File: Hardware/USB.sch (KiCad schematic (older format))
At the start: 11 parts

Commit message: [Hardware] Added USB-B connector reference and 3D model.
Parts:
- J1: renamed from J?; value USB_B -> 2411_06; Manufacturer (none) -> Lumberg
- gave numbers to parts that had none: 10
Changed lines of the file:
@@
 P 6600 3950
 AR Path="/61165087" Ref="U?"  Part="1"
-AR Path="/611612DA/61165087" Ref="U?"  Part="1"
-F 0 "U?" H 7000 3300 50  0000 C CNN
+AR Path="/611612DA/61165087" Ref="U1"  Part="1"
+F 0 "U1" H 7000 3300 50  0000 C CNN
 F 1 "FT230XS" H 7100 3200 50  0000 C CNN
 F 2 "Package_SO:SSOP-16_3.9x4.9mm_P0.635mm" H 7600 3350 50  0001 C CNN
@@
 P 4700 3850
 AR Path="/6116508E" Ref="R?"  Part="1"
-AR Path="/611612DA/6116508E" Ref="R?"  Part="1"
-F 0 "R?" V 4403 3850 50  0000 C CNN
+AR Path="/611612DA/6116508E" Ref="R1"  Part="1"
+F 0 "R1" V 4403 3850 50  0000 C CNN
 F 1 "27" V 4494 3850 50  0000 C CNN
 F 2 "Resistor_SMD:R_0603_1608Metric_Pad0.98x0.95mm_HandSolder" V 4630 3850 50  0001 C CNN
@@
 P 4700 3950
 AR Path="/61165095" Ref="R?"  Part="1"
-AR Path="/611612DA/61165095" Ref="R?"  Part="1"
-F 0 "R?" V 4815 3950 50  0000 C CNN
+AR Path="/611612DA/61165095" Ref="R2"  Part="1"
+F 0 "R2" V 4815 3950 50  0000 C CNN
 F 1 "27" V 4906 3950 50  0000 C CNN
 F 2 "Resistor_SMD:R_0603_1608Metric_Pad0.98x0.95mm_HandSolder" V 4630 3950 50  0001 C CNN
@@
 P 3900 4500
 AR Path="/6116509D" Ref="C?"  Part="1"
-AR Path="/611612DA/6116509D" Ref="C?"  Part="1"
-F 0 "C?" H 3786 4637 50  0000 R CNN
+AR Path="/611612DA/6116509D" Ref="C6"  Part="1"
+F 0 "C6" H 3786 4637 50  0000 R CNN
 F 1 "47p" H 3786 4546 50  0000 R CNN
 F 2 "Capacitor_SMD:C_0603_1608Metric_Pad1.08x0.95mm_HandSolder" H 3938 4350 50  0001 C CNN
@@
 P 4200 4500
 AR Path="/611650A5" Ref="C?"  Part="1"
-AR Path="/611612DA/611650A5" Ref="C?"  Part="1"
-F 0 "C?" H 4315 4637 50  0000 L CNN
+AR Path="/611612DA/611650A5" Ref="C7"  Part="1"
+F 0 "C7" H 4315 4637 50  0000 L CNN
 F 1 "47p" H 4315 4546 50  0000 L CNN
 F 2 "Capacitor_SMD:C_0603_1608Metric_Pad1.08x0.95mm_HandSolder" H 4238 4350 50  0001 C CNN
@@
 P 2900 3850
 AR Path="/611650AB" Ref="J?"  Part="1"
-AR Path="/611612DA/611650AB" Ref="J?"  Part="1"
-F 0 "J?" H 2957 4317 50  0000 C CNN
-F 1 "USB_B" H 2957 4226 50  0000 C CNN
+AR Path="/611612DA/611650AB" Ref="J1"  Part="1"
+F 0 "J1" H 2957 4317 50  0000 C CNN
+F 1 "2411_06" H 2957 4226 50  0000 C CNN
 F 2 "Connector_USB:USB_B_OST_USB-B1HSxx_Horizontal" H 3050 3800 50  0001 C CNN
 F 3 " ~" H 3050 3800 50  0001 C CNN
+F 4 "Lumberg" H 2900 3850 50  0001 C CNN "Manufacturer"
 	1    2900 3850
 	1    0    0    -1
 $EndComp
 $Comp
-L power:GND #PWR?
+L power:GND #PWR09
 U 1 1 61168B65
 P 6600 4800
-F 0 "#PWR?" H 6600 4550 50  0001 C CNN
+F 0 "#PWR09" H 6600 4550 50  0001 C CNN
 F 1 "GND" H 6605 4627 50  0000 C CNN
 F 2 "" H 6600 4800 50  0001 C CNN
@@
 Connection ~ 6600 4750
 $Comp
-L power:GND #PWR?
+L power:GND #PWR010
 U 1 1 61169C53
 P 4050 4850
-F 0 "#PWR?" H 4050 4600 50  0001 C CNN
+F 0 "#PWR010" H 4050 4600 50  0001 C CNN
 F 1 "GND" H 4055 4677 50  0000 C CNN
 F 2 "" H 4050 4850 50  0001 C CNN
@@
 USB_2_D+
 $Comp
-L power:GND #PWR?
+L power:GND #PWR08
 U 1 1 61185C32
 P 2850 4350
-F 0 "#PWR?" H 2850 4100 50  0001 C CNN
+F 0 "#PWR08" H 2850 4100 50  0001 C CNN
 F 1 "GND" H 2855 4177 50  0000 C CNN
 F 2 "" H 2850 4350 50  0001 C CNN
@@
 Connection ~ 2850 4300
 $Comp
-L power:+5V #PWR?
+L power:+5V #PWR05
 U 1 1 6118716E
 P 3300 3300
-F 0 "#PWR?" H 3300 3150 50  0001 C CNN
+F 0 "#PWR05" H 3300 3150 50  0001 C CNN
 F 1 "+5V" H 3315 3473 50  0000 C CNN
 F 2 "" H 3300 3300 50  0001 C CNN
@@
 P 6050 2600
 AR Path="/611938BC" Ref="C?"  Part="1"
-AR Path="/611612DA/611938BC" Ref="C?"  Part="1"
-F 0 "C?" H 6165 2737 50  0000 L CNN
+AR Path="/611612DA/611938BC" Ref="C4"  Part="1"
+F 0 "C4" H 6165 2737 50  0000 L CNN
 F 1 "4.7u" H 6165 2646 50  0000 L CNN
 F 2 "Capacitor_SMD:C_0805_2012Metric_Pad1.18x1.45mm_HandSolder" H 6088 2450 50  0001 C CNN
@@
 P 5500 2600
 AR Path="/61195755" Ref="C?"  Part="1"
-AR Path="/611612DA/61195755" Ref="C?"  Part="1"
-F 0 "C?" H 5615 2737 50  0000 L CNN
+AR Path="/611612DA/61195755" Ref="C3"  Part="1"
+F 0 "C3" H 5615 2737 50  0000 L CNN
 F 1 "4.7u" H 5615 2646 50  0000 L CNN
 F 2 "Capacitor_SMD:C_0805_2012Metric_Pad1.18x1.45mm_HandSolder" H 5538 2450 50  0001 C CNN
@@
 P 4950 2600
 AR Path="/61196FE9" Ref="C?"  Part="1"
-AR Path="/611612DA/61196FE9" Ref="C?"  Part="1"
-F 0 "C?" H 5065 2737 50  0000 L CNN
+AR Path="/611612DA/61196FE9" Ref="C2"  Part="1"
+F 0 "C2" H 5065 2737 50  0000 L CNN
 F 1 "100n" H 5065 2646 50  0000 L CNN
 F 2 "Capacitor_SMD:C_0603_1608Metric_Pad1.08x0.95mm_HandSolder" H 4988 2450 50  0001 C CNN
@@
 P 4400 2600
 AR Path="/6119756B" Ref="C?"  Part="1"
-AR Path="/611612DA/6119756B" Ref="C?"  Part="1"
-F 0 "C?" H 4515 2737 50  0000 L CNN
+AR Path="/611612DA/6119756B" Ref="C1"  Part="1"
+F 0 "C1" H 4515 2737 50  0000 L CNN
 F 1 "100n" H 4515 2646 50  0000 L CNN
 F 2 "Capacitor_SMD:C_0603_1608Metric_Pad1.08x0.95mm_HandSolder" H 4438 2450 50  0001 C CNN
@@
 $EndComp
 $Comp
-L power:+5V #PWR?
+L power:+5V #PWR01
 U 1 1 611A0261
 P 4400 2250
-F 0 "#PWR?" H 4400 2100 50  0001 C CNN
+F 0 "#PWR01" H 4400 2100 50  0001 C CNN
 F 1 "+5V" H 4415 2423 50  0000 C CNN
 F 2 "" H 4400 2250 50  0001 C CNN
@@
 	6500 2350 6500 3250
 $Comp
-L power:GND #PWR?
+L power:GND #PWR04
 U 1 1 611A5DF9
 P 5250 2950
-F 0 "#PWR?" H 5250 2700 50  0001 C CNN
+F 0 "#PWR04" H 5250 2700 50  0001 C CNN
 F 1 "GND" H 5255 2777 50  0000 C CNN
 F 2 "" H 5250 2950 50  0001 C CNN
@@
 	5250 2850 5500 2850
 $Comp
-L power:+3.3VA #PWR?
+L power:+3.3VA #PWR02
 U 1 1 611A8920
 P 7100 2250
-F 0 "#PWR?" H 7100 2100 50  0001 C CNN
+F 0 "#PWR02" H 7100 2100 50  0001 C CNN
 F 1 "+3.3VA" H 7115 2423 50  0000 C CNN
 F 2 "" H 7100 2250 50  0001 C CNN
@@
 P 7100 2600
 AR Path="/611A99B1" Ref="C?"  Part="1"
-AR Path="/611612DA/611A99B1" Ref="C?"  Part="1"
-F 0 "C?" H 7215 2737 50  0000 L CNN
+AR Path="/611612DA/611A99B1" Ref="C5"  Part="1"
+F 0 "C5" H 7215 2737 50  0000 L CNN
 F 1 "100n" H 7215 2646 50  0000 L CNN
 F 2 "Capacitor_SMD:C_0603_1608Metric_Pad1.08x0.95mm_HandSolder" H 7138 2450 50  0001 C CNN
@@
 Connection ~ 7100 2350
 $Comp
-L power:GND #PWR?
+L power:GND #PWR03
 U 1 1 611ACC4D
 P 7100 2850
-F 0 "#PWR?" H 7100 2600 50  0001 C CNN
+F 0 "#PWR03" H 7100 2600 50  0001 C CNN
 F 1 "GND" H 7105 2677 50  0000 C CNN
 F 2 "" H 7100 2850 50  0001 C CNN
@@
 	7100 2850 7100 2750
 $Comp
-L power:+3.3VA #PWR?
+L power:+3.3VA #PWR06
 U 1 1 611AF903
 P 5800 3550
-F 0 "#PWR?" H 5800 3400 50  0001 C CNN
+F 0 "#PWR06" H 5800 3400 50  0001 C CNN
 F 1 "+3.3VA" V 5815 3677 50  0000 L CNN
 F 2 "" H 5800 3550 50  0001 C CNN
@@
 $EndComp
 $Comp
-L power:+3.3VA #PWR?
+L power:+3.3VA #PWR07
 U 1 1 611B03B1
 P 5800 4150
-F 0 "#PWR?" H 5800 4000 50  0001 C CNN
+F 0 "#PWR07" H 5800 4000 50  0001 C CNN
 F 1 "+3.3VA" V 5815 4277 50  0000 L CNN
 F 2 "" H 5800 4150 50  0001 C CNN

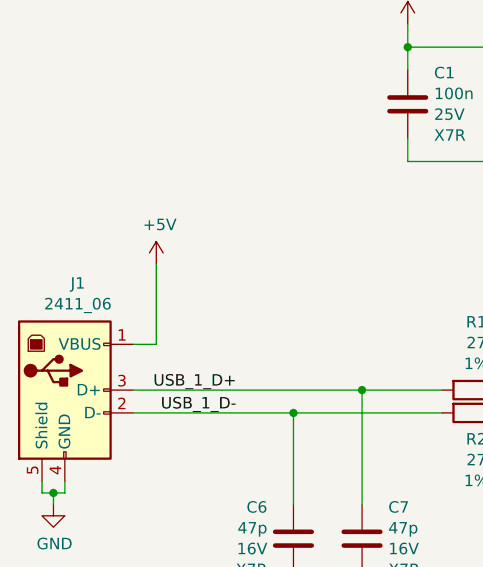
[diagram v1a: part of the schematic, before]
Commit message: [Hardware] Added relays schematic sheet.
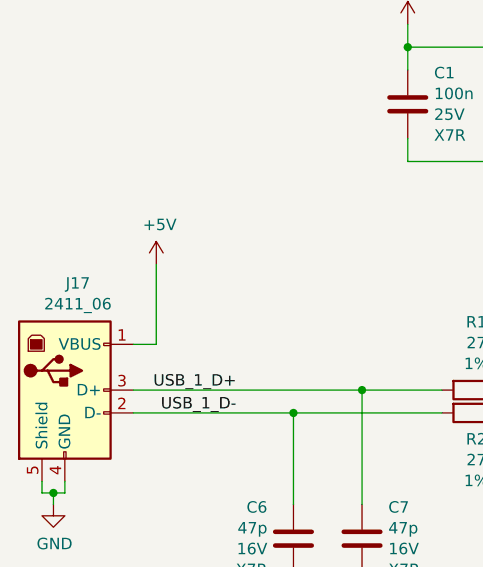
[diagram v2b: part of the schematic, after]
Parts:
- renumbered J1 to J17
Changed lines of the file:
@@
 P 2900 3850
 AR Path="/611650AB" Ref="J?"  Part="1"
-AR Path="/611612DA/611650AB" Ref="J1"  Part="1"
-F 0 "J1" H 2957 4317 50  0000 C CNN
+AR Path="/611612DA/611650AB" Ref="J17"  Part="1"
+F 0 "J17" H 2957 4317 50  0000 C CNN
 F 1 "2411_06" H 2957 4226 50  0000 C CNN
 F 2 "Connector_USB:USB_B_OST_USB-B1HSxx_Horizontal" H 3050 3800 50  0001 C CNN

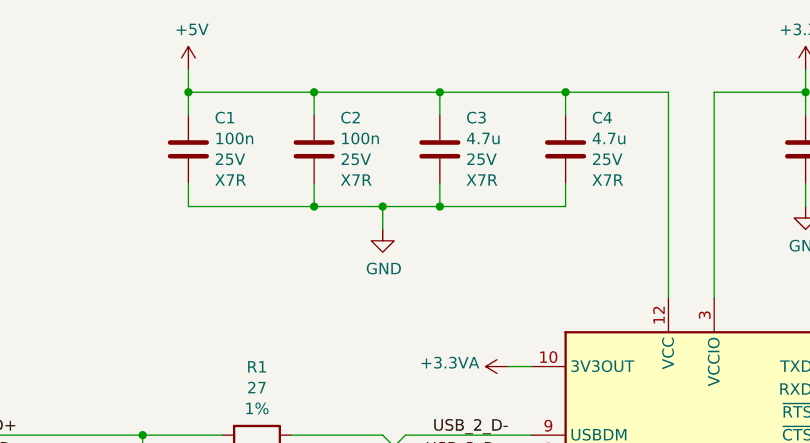
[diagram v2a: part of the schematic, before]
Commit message: [Hardware] Positioned components on PCB.
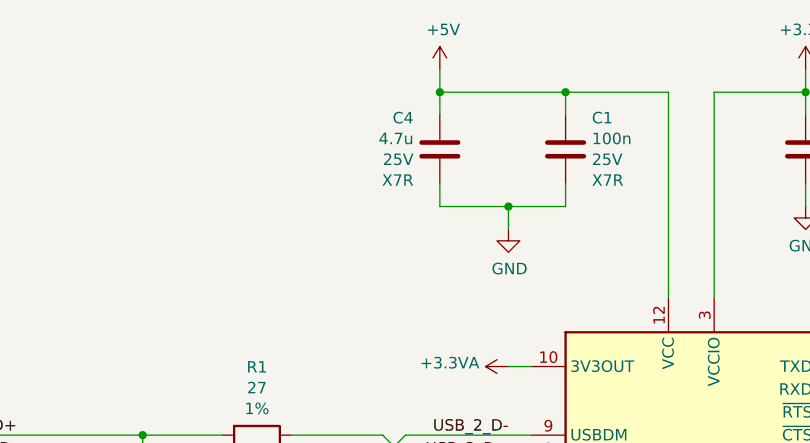
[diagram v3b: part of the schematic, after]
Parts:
- removed C2: 100n, Capacitor_SMD:C_0603_1608Metric_Pad1.08x0.95mm_HandSolder, symbol Device:C
- removed C3: 4.7u, Capacitor_SMD:C_0805_2012Metric_Pad1.18x1.45mm_HandSolder, symbol Device:C
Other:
- moved on the sheet: C1, C4
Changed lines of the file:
@@
 L Device:C C?
 U 1 1 611938BC
-P 6050 2600
+P 5500 2600
 AR Path="/611938BC" Ref="C?"  Part="1"
 AR Path="/611612DA/611938BC" Ref="C4"  Part="1"
-F 0 "C4" H 6165 2737 50  0000 L CNN
-F 1 "4.7u" H 6165 2646 50  0000 L CNN
-F 2 "Capacitor_SMD:C_0805_2012Metric_Pad1.18x1.45mm_HandSolder" H 6088 2450 50  0001 C CNN
+F 0 "C4" H 5385 2737 50  0000 R CNN
+F 1 "4.7u" H 5385 2646 50  0000 R CNN
+F 2 "Capacitor_SMD:C_0805_2012Metric_Pad1.18x1.45mm_HandSolder" H 5538 2450 50  0001 C CNN
+F 3 "~" H 5500 2600 50  0001 C CNN
+F 4 "25V" H 5385 2555 50  0000 R CNN "Value2"
+F 5 "X7R" H 5385 2464 50  0000 R CNN "Value3"
+	1    5500 2600
+	1    0    0    -1
+$EndComp
+$Comp
+L Device:C C?
+U 1 1 6119756B
+P 6050 2600
+AR Path="/6119756B" Ref="C?"  Part="1"
+AR Path="/611612DA/6119756B" Ref="C1"  Part="1"
+F 0 "C1" H 6165 2737 50  0000 L CNN
+F 1 "100n" H 6165 2646 50  0000 L CNN
+F 2 "Capacitor_SMD:C_0603_1608Metric_Pad1.08x0.95mm_HandSolder" H 6088 2450 50  0001 C CNN
 F 3 "~" H 6050 2600 50  0001 C CNN
 F 4 "25V" H 6165 2555 50  0000 L CNN "Value2"
@@
 $EndComp
 $Comp
-L Device:C C?
-U 1 1 61195755
-P 5500 2600
-AR Path="/61195755" Ref="C?"  Part="1"
-AR Path="/611612DA/61195755" Ref="C3"  Part="1"
-F 0 "C3" H 5615 2737 50  0000 L CNN
-F 1 "4.7u" H 5615 2646 50  0000 L CNN
-F 2 "Capacitor_SMD:C_0805_2012Metric_Pad1.18x1.45mm_HandSolder" H 5538 2450 50  0001 C CNN
-F 3 "~" H 5500 2600 50  0001 C CNN
-F 4 "25V" H 5615 2555 50  0000 L CNN "Value2"
-F 5 "X7R" H 5615 2464 50  0000 L CNN "Value3"
-	1    5500 2600
-	1    0    0    -1
-$EndComp
-$Comp
-L Device:C C?
-U 1 1 61196FE9
-P 4950 2600
-AR Path="/61196FE9" Ref="C?"  Part="1"
-AR Path="/611612DA/61196FE9" Ref="C2"  Part="1"
-F 0 "C2" H 5065 2737 50  0000 L CNN
-F 1 "100n" H 5065 2646 50  0000 L CNN
-F 2 "Capacitor_SMD:C_0603_1608Metric_Pad1.08x0.95mm_HandSolder" H 4988 2450 50  0001 C CNN
-F 3 "~" H 4950 2600 50  0001 C CNN
-F 4 "25V" H 5065 2555 50  0000 L CNN "Value2"
-F 5 "X7R" H 5065 2464 50  0000 L CNN "Value3"
-	1    4950 2600
-	1    0    0    -1
-$EndComp
-$Comp
-L Device:C C?
-U 1 1 6119756B
-P 4400 2600
-AR Path="/6119756B" Ref="C?"  Part="1"
-AR Path="/611612DA/6119756B" Ref="C1"  Part="1"
-F 0 "C1" H 4515 2737 50  0000 L CNN
-F 1 "100n" H 4515 2646 50  0000 L CNN
-F 2 "Capacitor_SMD:C_0603_1608Metric_Pad1.08x0.95mm_HandSolder" H 4438 2450 50  0001 C CNN
-F 3 "~" H 4400 2600 50  0001 C CNN
-F 4 "25V" H 4515 2555 50  0000 L CNN "Value2"
-F 5 "X7R" H 4515 2464 50  0000 L CNN "Value3"
-	1    4400 2600
-	1    0    0    -1
-$EndComp
-$Comp
 L power:+5V #PWR01
 U 1 1 611A0261
-P 4400 2250
-F 0 "#PWR01" H 4400 2100 50  0001 C CNN
-F 1 "+5V" H 4415 2423 50  0000 C CNN
-F 2 "" H 4400 2250 50  0001 C CNN
-F 3 "" H 4400 2250 50  0001 C CNN
-	1    4400 2250
+P 5500 2250
+F 0 "#PWR01" H 5500 2100 50  0001 C CNN
+F 1 "+5V" H 5515 2423 50  0000 C CNN
+F 2 "" H 5500 2250 50  0001 C CNN
+F 3 "" H 5500 2250 50  0001 C CNN
+	1    5500 2250
 	1    0    0    -1
 $EndComp
 Wire Wire Line
-	4400 2450 4400 2350
-Wire Wire Line
-	4400 2350 4950 2350
-Wire Wire Line
-	4950 2350 4950 2450
-Wire Wire Line
-	4950 2350 5500 2350
-Wire Wire Line
 	5500 2350 5500 2450
-Connection ~ 4950 2350
 Wire Wire Line
 	6050 2350 6050 2450
 Connection ~ 5500 2350
 Wire Wire Line
-	4400 2250 4400 2350
-Connection ~ 4400 2350
+	5500 2850 5500 2750
 Wire Wire Line
-	4400 2750 4400 2850
-Wire Wire Line
-	4400 2850 4950 2850
-Wire Wire Line
-	4950 2850 4950 2750
-Wire Wire Line
-	4950 2850 5250 2850
-Wire Wire Line
-	5500 2850 5500 2750
-Connection ~ 4950 2850
-Wire Wire Line
-	5500 2850 6050 2850
+	5500 2850 5800 2850
 Wire Wire Line
 	6050 2850 6050 2750
-Connection ~ 5500 2850
 Wire Wire Line
 	5500 2350 6050 2350
@@
 L power:GND #PWR04
 U 1 1 611A5DF9
-P 5250 2950
-F 0 "#PWR04" H 5250 2700 50  0001 C CNN
-F 1 "GND" H 5255 2777 50  0000 C CNN
-F 2 "" H 5250 2950 50  0001 C CNN
-F 3 "" H 5250 2950 50  0001 C CNN
-	1    5250 2950
+P 5800 2950
+F 0 "#PWR04" H 5800 2700 50  0001 C CNN
+F 1 "GND" H 5805 2777 50  0000 C CNN
+F 2 "" H 5800 2950 50  0001 C CNN
+F 3 "" H 5800 2950 50  0001 C CNN
+	1    5800 2950
 	1    0    0    -1
 $EndComp
-Wire Wire Line
-	5250 2850 5250 2950
-Connection ~ 5250 2850
-Wire Wire Line
-	5250 2850 5500 2850
 $Comp
 L power:+3.3VA #PWR02
@@
 Text Notes 4850 4900 0    50   ~ 0
 USB 2.0 lines must be\nrouted with 90ohms impedance.
+Wire Wire Line
+	5500 2350 5500 2250
+Wire Wire Line
+	5800 2950 5800 2850
+Connection ~ 5800 2850
+Wire Wire Line
+	5800 2850 6050 2850
 $EndSCHEMATC

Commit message: [Hardware] Renamed components in a more coherent way.
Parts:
- renumbered C1 to C5, C5 to C6, C6 to C7, C7 to C8, J17 to J18, R1 to R20, R2 to R21, U1 to U2
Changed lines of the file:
@@
 P 6600 3950
 AR Path="/61165087" Ref="U?"  Part="1"
-AR Path="/611612DA/61165087" Ref="U1"  Part="1"
-F 0 "U1" H 7000 3300 50  0000 C CNN
+AR Path="/611612DA/61165087" Ref="U2"  Part="1"
+F 0 "U2" H 7000 3300 50  0000 C CNN
 F 1 "FT230XS" H 7100 3200 50  0000 C CNN
 F 2 "Package_SO:SSOP-16_3.9x4.9mm_P0.635mm" H 7600 3350 50  0001 C CNN
@@
 P 4700 3850
 AR Path="/6116508E" Ref="R?"  Part="1"
-AR Path="/611612DA/6116508E" Ref="R1"  Part="1"
-F 0 "R1" V 4403 3850 50  0000 C CNN
+AR Path="/611612DA/6116508E" Ref="R20"  Part="1"
+F 0 "R20" V 4403 3850 50  0000 C CNN
 F 1 "27" V 4494 3850 50  0000 C CNN
 F 2 "Resistor_SMD:R_0603_1608Metric_Pad0.98x0.95mm_HandSolder" V 4630 3850 50  0001 C CNN
@@
 P 4700 3950
 AR Path="/61165095" Ref="R?"  Part="1"
-AR Path="/611612DA/61165095" Ref="R2"  Part="1"
-F 0 "R2" V 4815 3950 50  0000 C CNN
+AR Path="/611612DA/61165095" Ref="R21"  Part="1"
+F 0 "R21" V 4815 3950 50  0000 C CNN
 F 1 "27" V 4906 3950 50  0000 C CNN
 F 2 "Resistor_SMD:R_0603_1608Metric_Pad0.98x0.95mm_HandSolder" V 4630 3950 50  0001 C CNN
@@
 P 3900 4500
 AR Path="/6116509D" Ref="C?"  Part="1"
-AR Path="/611612DA/6116509D" Ref="C6"  Part="1"
-F 0 "C6" H 3786 4637 50  0000 R CNN
+AR Path="/611612DA/6116509D" Ref="C7"  Part="1"
+F 0 "C7" H 3786 4637 50  0000 R CNN
 F 1 "47p" H 3786 4546 50  0000 R CNN
 F 2 "Capacitor_SMD:C_0603_1608Metric_Pad1.08x0.95mm_HandSolder" H 3938 4350 50  0001 C CNN
@@
 P 4200 4500
 AR Path="/611650A5" Ref="C?"  Part="1"
-AR Path="/611612DA/611650A5" Ref="C7"  Part="1"
-F 0 "C7" H 4315 4637 50  0000 L CNN
+AR Path="/611612DA/611650A5" Ref="C8"  Part="1"
+F 0 "C8" H 4315 4637 50  0000 L CNN
 F 1 "47p" H 4315 4546 50  0000 L CNN
 F 2 "Capacitor_SMD:C_0603_1608Metric_Pad1.08x0.95mm_HandSolder" H 4238 4350 50  0001 C CNN
@@
 P 2900 3850
 AR Path="/611650AB" Ref="J?"  Part="1"
-AR Path="/611612DA/611650AB" Ref="J17"  Part="1"
-F 0 "J17" H 2957 4317 50  0000 C CNN
+AR Path="/611612DA/611650AB" Ref="J18"  Part="1"
+F 0 "J18" H 2957 4317 50  0000 C CNN
 F 1 "2411_06" H 2957 4226 50  0000 C CNN
 F 2 "Connector_USB:USB_B_OST_USB-B1HSxx_Horizontal" H 3050 3800 50  0001 C CNN
@@
 $EndComp
 $Comp
-L power:GND #PWR09
+L power:GND #PWR041
 U 1 1 61168B65
 P 6600 4800
-F 0 "#PWR09" H 6600 4550 50  0001 C CNN
+F 0 "#PWR041" H 6600 4550 50  0001 C CNN
 F 1 "GND" H 6605 4627 50  0000 C CNN
 F 2 "" H 6600 4800 50  0001 C CNN
@@
 Connection ~ 6600 4750
 $Comp
-L power:GND #PWR010
+L power:GND #PWR042
 U 1 1 61169C53
 P 4050 4850
-F 0 "#PWR010" H 4050 4600 50  0001 C CNN
+F 0 "#PWR042" H 4050 4600 50  0001 C CNN
 F 1 "GND" H 4055 4677 50  0000 C CNN
 F 2 "" H 4050 4850 50  0001 C CNN
@@
 USB_2_D+
 $Comp
-L power:GND #PWR08
+L power:GND #PWR040
 U 1 1 61185C32
 P 2850 4350
-F 0 "#PWR08" H 2850 4100 50  0001 C CNN
+F 0 "#PWR040" H 2850 4100 50  0001 C CNN
 F 1 "GND" H 2855 4177 50  0000 C CNN
 F 2 "" H 2850 4350 50  0001 C CNN
@@
 Connection ~ 2850 4300
 $Comp
-L power:+5V #PWR05
+L power:+5V #PWR037
 U 1 1 6118716E
 P 3300 3300
-F 0 "#PWR05" H 3300 3150 50  0001 C CNN
+F 0 "#PWR037" H 3300 3150 50  0001 C CNN
 F 1 "+5V" H 3315 3473 50  0000 C CNN
 F 2 "" H 3300 3300 50  0001 C CNN
@@
 P 6050 2600
 AR Path="/6119756B" Ref="C?"  Part="1"
-AR Path="/611612DA/6119756B" Ref="C1"  Part="1"
-F 0 "C1" H 6165 2737 50  0000 L CNN
+AR Path="/611612DA/6119756B" Ref="C5"  Part="1"
+F 0 "C5" H 6165 2737 50  0000 L CNN
 F 1 "100n" H 6165 2646 50  0000 L CNN
 F 2 "Capacitor_SMD:C_0603_1608Metric_Pad1.08x0.95mm_HandSolder" H 6088 2450 50  0001 C CNN
@@
 $EndComp
 $Comp
-L power:+5V #PWR01
+L power:+5V #PWR033
 U 1 1 611A0261
 P 5500 2250
-F 0 "#PWR01" H 5500 2100 50  0001 C CNN
+F 0 "#PWR033" H 5500 2100 50  0001 C CNN
 F 1 "+5V" H 5515 2423 50  0000 C CNN
 F 2 "" H 5500 2250 50  0001 C CNN
@@
 	6500 2350 6500 3250
 $Comp
-L power:GND #PWR04
+L power:GND #PWR036
 U 1 1 611A5DF9
 P 5800 2950
-F 0 "#PWR04" H 5800 2700 50  0001 C CNN
+F 0 "#PWR036" H 5800 2700 50  0001 C CNN
 F 1 "GND" H 5805 2777 50  0000 C CNN
 F 2 "" H 5800 2950 50  0001 C CNN
@@
 $EndComp
 $Comp
-L power:+3.3VA #PWR02
+L power:+3.3VA #PWR034
 U 1 1 611A8920
 P 7100 2250
-F 0 "#PWR02" H 7100 2100 50  0001 C CNN
+F 0 "#PWR034" H 7100 2100 50  0001 C CNN
 F 1 "+3.3VA" H 7115 2423 50  0000 C CNN
 F 2 "" H 7100 2250 50  0001 C CNN
@@
 P 7100 2600
 AR Path="/611A99B1" Ref="C?"  Part="1"
-AR Path="/611612DA/611A99B1" Ref="C5"  Part="1"
-F 0 "C5" H 7215 2737 50  0000 L CNN
+AR Path="/611612DA/611A99B1" Ref="C6"  Part="1"
+F 0 "C6" H 7215 2737 50  0000 L CNN
 F 1 "100n" H 7215 2646 50  0000 L CNN
 F 2 "Capacitor_SMD:C_0603_1608Metric_Pad1.08x0.95mm_HandSolder" H 7138 2450 50  0001 C CNN
@@
 Connection ~ 7100 2350
 $Comp
-L power:GND #PWR03
+L power:GND #PWR035
 U 1 1 611ACC4D
 P 7100 2850
-F 0 "#PWR03" H 7100 2600 50  0001 C CNN
+F 0 "#PWR035" H 7100 2600 50  0001 C CNN
 F 1 "GND" H 7105 2677 50  0000 C CNN
 F 2 "" H 7100 2850 50  0001 C CNN
@@
 	7100 2850 7100 2750
 $Comp
-L power:+3.3VA #PWR06
+L power:+3.3VA #PWR038
 U 1 1 611AF903
 P 5800 3550
-F 0 "#PWR06" H 5800 3400 50  0001 C CNN
+F 0 "#PWR038" H 5800 3400 50  0001 C CNN
 F 1 "+3.3VA" V 5815 3677 50  0000 L CNN
 F 2 "" H 5800 3550 50  0001 C CNN
@@
 $EndComp
 $Comp
-L power:+3.3VA #PWR07
+L power:+3.3VA #PWR039
 U 1 1 611B03B1
 P 5800 4150
-F 0 "#PWR07" H 5800 4000 50  0001 C CNN
+F 0 "#PWR039" H 5800 4000 50  0001 C CNN
 F 1 "+3.3VA" V 5815 4277 50  0000 L CNN
 F 2 "" H 5800 4150 50  0001 C CNN
